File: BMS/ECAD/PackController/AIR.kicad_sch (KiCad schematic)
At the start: 0 parts

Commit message: did AIR monitoring circuit and started SDC CTRL / logik
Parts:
- added C401: 100nC 6V, Capacitor_SMD:C_0603_1608Metric, symbol Device:C
- added D401, D402: BAS16HT1G, Diode_SMD:D_SOD-323F, symbol Device:D
- added J1: Conn_01x08, symbol Connector_Generic:Conn_01x08
- added K401: AIR_P, symbol Relay:DIPxx-2Axx-21x
- added K402: AIR_N, symbol Relay:DIPxx-2Axx-21x
- added Q401, Q403: BC847C, Package_TO_SOT_SMD:SOT-23-3, symbol Transistor_BJT:Q_NPN_BEC
- added Q402, Q404: DMP4065S-7, Package_TO_SOT_SMD:SOT-23-3, symbol Transistor_FET:Q_PMOS_GSD
- added R401, R402, R407, R408, R409, R410, R411, R412, R413, R414: 1kR, Resistor_SMD:R_0603_1608Metric, symbol Device:R
- added R403, R405, R415, R417, R418, R419, R421, R422: 10kR, Resistor_SMD:R_0603_1608Metric, symbol Device:R
- added R404, R406: 1k5R, Resistor_SMD:R_0603_1608Metric, symbol Device:R
- added R416, R420: 4k7R, Resistor_SMD:R_0603_1608Metric, symbol Device:R
- added U401: ADCMP393ARUZ, symbol EKartParts:ADCMP393ARUZ
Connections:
- new net: R409.1, R410.2, U401.5 (+), U401.9 (+)
- new net: Q404.1 (G), R421.2, R422.1
- new net: Q403.3 (C), R422.2
- new net: R410.1, R411.2, U401.11 (+), U401.7 (+)
- new net: Q402.1 (G), R417.1, R418.2
- new net: Q401.3 (C), R417.2
- new net +3.3V: C401.1, R407.2, R408.2, R409.2, R412.2, R413.2, R414.2, U401.3 (VCC)
- new net AIR_Error: R412.1, U401.1, U401.13
- new net AIR_N_AUX1: J1.8 (Pin_8), K402.14, R407.1, U401.10 (-), U401.8 (-)
- new net AIR_N_AUX2: J1.4 (Pin_4), K402.8, R402.2
- new net AIR_N_Enable: D401.1 (K), J1.6 (Pin_6), K402.2, Q404.3 (D), R405.2
- new net AIR_N_Intended: R405.1, R406.1
- new net AIR_P_AUX1: J1.7 (Pin_7), K401.14, R408.1, U401.4 (-), U401.6 (-)
- new net AIR_P_AUX2: J1.3 (Pin_3), K401.8, R401.2
- new net AIR_P_Actual: R413.1, R414.1, U401.14, U401.2
- new net AIR_P_Enable: D402.1 (K), J1.5 (Pin_5), K401.2, Q402.3 (D), R403.2
- new net AIR_P_Intended: R403.1, R404.1
- new net GND: C401.2, D401.2 (A), D402.2 (A), J1.1 (Pin_1), J1.2 (Pin_2), K401.6, K402.6, Q401.2 (E), Q403.2 (E), R401.1, R402.1, R404.2, R406.2, R411.1, R415.2, R419.2, U401.12 (GND)
- new net SC_END: Q402.2 (S), Q404.2 (S), R418.1, R421.1
- new net TS_N_External: K402.7
- new net TS_N_Internal: K402.1
- new net TS_P_External: K401.7
- new net TS_P_Internal: K401.1
- new net ÂIR_N_Switch: R419.1, R420.2
- new net ÂIR_P_Switch: R415.1, R416.2

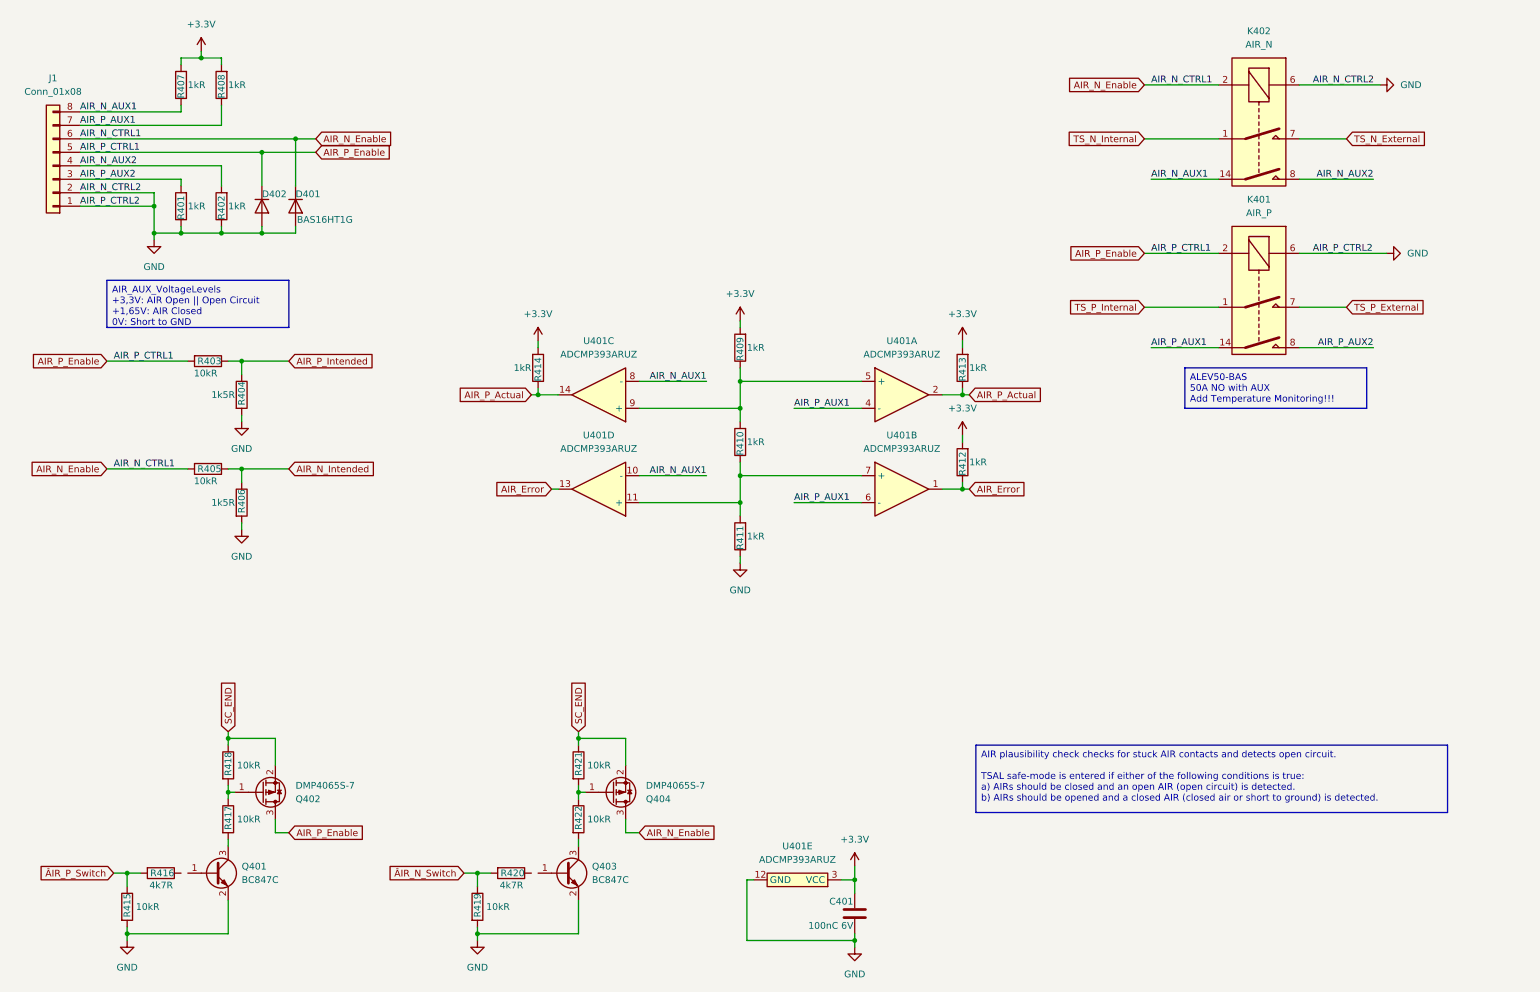
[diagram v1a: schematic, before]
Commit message: IMD control circuit
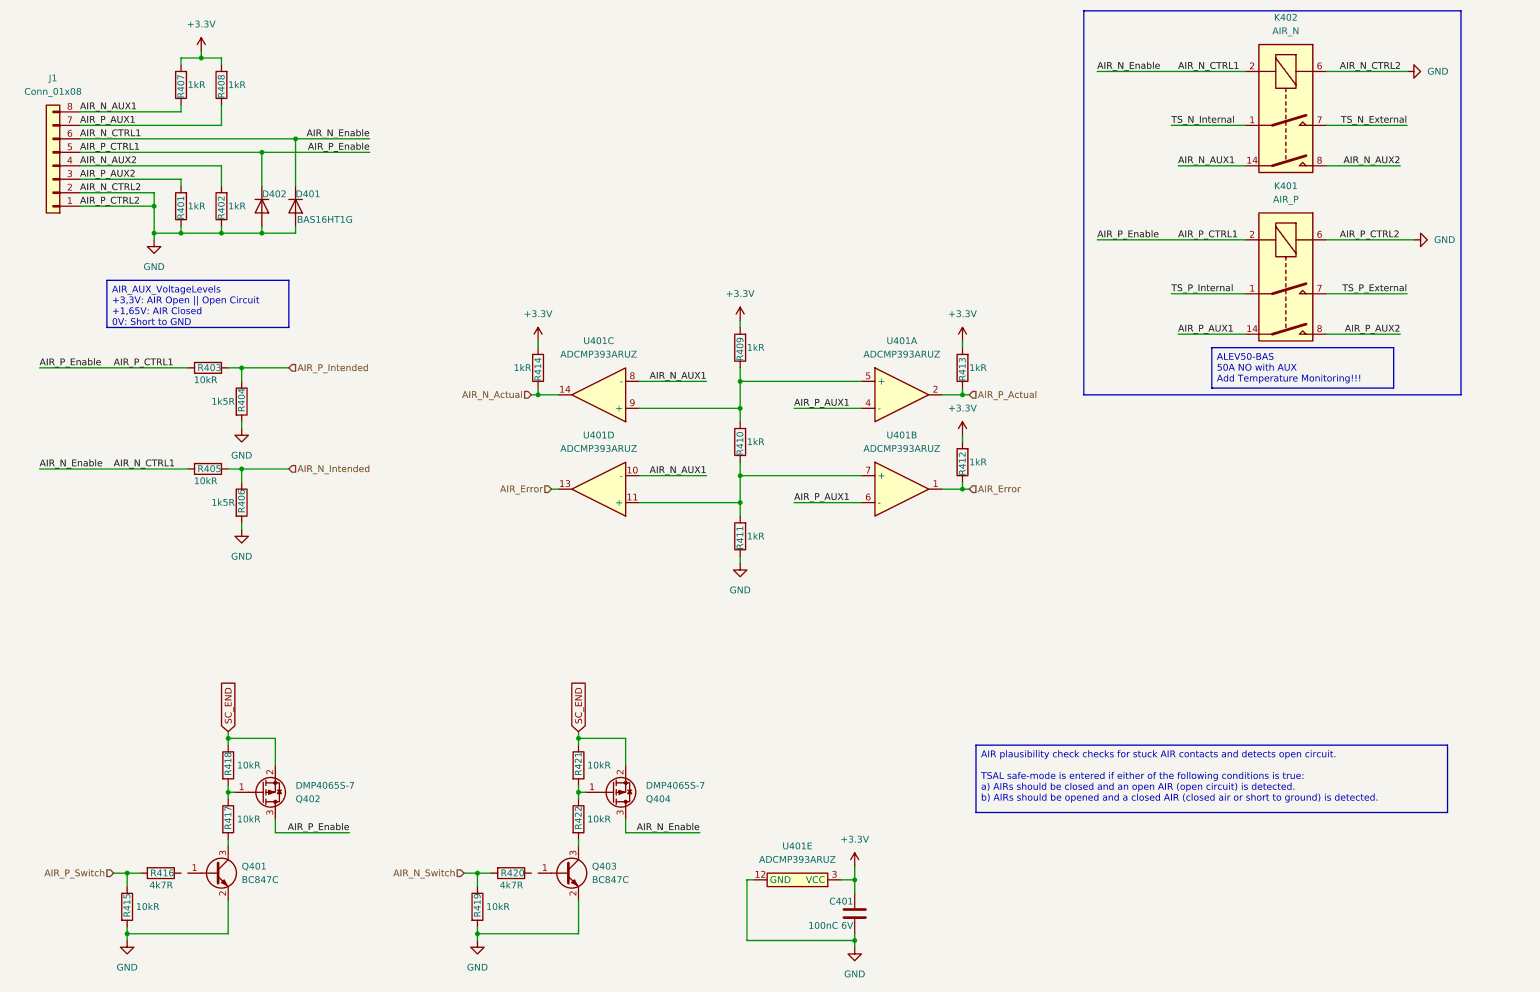
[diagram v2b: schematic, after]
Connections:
- net AIR_P_Actual: no longer R414.1, U401.14
- net AIR_N_Enable renamed AIR_N_CTRL1
- net AIR_P_Enable renamed AIR_P_CTRL1
- net ÂIR_N_Switch renamed AIR_N_Switch
- net ÂIR_P_Switch renamed AIR_P_Switch
- new net AIR_N_Actual: R414.1, U401.14
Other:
- moved on the sheet: K401, K402, R403, R404

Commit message: pack controller close to finished and startet pack controller
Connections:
- net at R420.1: now also Q403.1 (B)
- net at Q401.1 (B): now also R416.1

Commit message: finished schemativ of precharge
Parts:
- removed Q401, Q403: BC847C, Package_TO_SOT_SMD:SOT-23-3, symbol Transistor_BJT:Q_NPN_BEC
- added Q3, Q4: BC846, Package_TO_SOT_SMD:SOT-23, symbol Transistor_BJT:BC846
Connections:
- net GND: now also Q3.2 (E), Q4.2 (E)
- net at R422.2: now also Q4.3 (C)
- net at R420.1: now also Q4.1 (B)
- net at R416.1: now also Q3.1 (B)
- net at R417.2: now also Q3.3 (C)
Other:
- title: (none) -> PackController
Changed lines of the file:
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@@
 	(paper "A4")
 	(title_block
+		(title "PackController")
 		(date "2026-03-03")
 		(rev "V0.9")
@@
 		)
 	)
-	(global_label "SC_END"
+	(hierarchical_label "AIR_P_Actual"
 		(shape input)
-		(at 118.11 148.59 90)
-		(fields_autoplaced yes)
+		(at 191.77 85.09 0)
 		(effects
 			(font
@@
 			(justify left)
 		)
-		(property "Intersheetrefs" "${INTERSHEET_REFS}"
-			(at 118.11 138.4082 90)
-			(hide yes)
-			(show_name no)
-			(do_not_autoplace no)
-			(effects
-				(font
-					(size 1.27 1.27)
-				)
-				(justify left)
-			)
-		)
 	)
-	(global_label "SC_END"
+	(hierarchical_label "SC_END"
 		(shape input)
 		(at 52.07 148.59 90)
-		(fields_autoplaced yes)
 		(effects
 			(font
@@
 			(justify left)
 		)
-		(property "Intersheetrefs" "${INTERSHEET_REFS}"
-			(at 52.07 138.4082 90)
-			(hide yes)
-			(show_name no)
-			(do_not_autoplace no)
-			(effects
-				(font
-					(size 1.27 1.27)
-				)
-				(justify left)
-			)
-		)
 	)
-	(hierarchical_label "AIR_P_Actual"
+	(hierarchical_label "AIR_N_Actual"
 		(shape input)
-		(at 191.77 85.09 0)
+		(at 109.22 85.09 180)
 		(effects
 			(font
 				(size 1.27 1.27)
 			)
-			(justify left)
+			(justify right)
 		)
 	)
-	(hierarchical_label "AIR_N_Actual"
+	(hierarchical_label "SC_END"
 		(shape input)
-		(at 109.22 85.09 180)
+		(at 118.11 148.59 90)
 		(effects
 			(font
 				(size 1.27 1.27)
 			)
-			(justify right)
+			(justify left)
 		)
 	)
@@
 	)
 	(symbol
-		(lib_id "Transistor_BJT:Q_NPN_BEC")
+		(lib_id "Transistor_BJT:BC846")
 		(at 115.57 175.26 0)
 		(unit 1)
@@
 		(dnp no)
 		(fields_autoplaced yes)
-		(property "Reference" "Q403"
+		(property "Reference" "Q4"
 			(at 120.65 173.9899 0)
 			(show_name no)
@@
 			)
 		)
-		(property "Value" "BC847C"
+		(property "Value" "BC846"
 			(at 120.65 176.5299 0)
 			(show_name no)
@@
 			)
 		)
-		(property "Footprint" "Package_TO_SOT_SMD:SOT-23-3"
-			(at 120.65 172.72 0)
+		(property "Footprint" "Package_TO_SOT_SMD:SOT-23"
+			(at 120.65 177.165 0)
 			(hide yes)
 			(show_name no)
@@
 				(font
 					(size 1.27 1.27)
+					(italic yes)
 				)
+				(justify left)
 			)
 		)
-		(property "Datasheet" ""
+		(property "Datasheet" "https://assets.nexperia.com/documents/data-sheet/BC846_SER.pdf"
 			(at 115.57 175.26 0)
 			(hide yes)
@@
 					(size 1.27 1.27)
 				)
+				(justify left)
 			)
 		)
-		(property "Description" "NPN transistor, base/emitter/collector"
+		(property "Description" "0.1A Ic, 65V Vce, NPN Transistor, SOT-23"
 			(at 115.57 175.26 0)
 			(hide yes)
@@
 		(pin "2"
 		)
-		(pin "3"
-		)
 		(pin "1"
 		)
+		(pin "3"
+		)
 		(instances
 			(project "Pack_Controller"
 				(path "/58a1c93e-baba-4d23-9191-955e00968735/9e3af51c-36cf-42ea-bd79-21f3fecec64c"
-					(reference "Q403")
+					(reference "Q4")
 					(unit 1)
 				)
@@
 	)
 	(symbol
-		(lib_id "Transistor_BJT:Q_NPN_BEC")
-		(at 49.53 175.26 0)
-		(unit 1)
-		(body_style 1)
-		(exclude_from_sim no)
-		(in_bom yes)
-		(on_board yes)
-		(in_pos_files yes)
-		(dnp no)
-		(fields_autoplaced yes)
-		(property "Reference" "Q401"
-			(at 54.61 173.9899 0)
-			(show_name no)
-			(do_not_autoplace no)
-			(effects
-				(font
-					(size 1.27 1.27)
-				)
-				(justify left)
-			)
-		)
-		(property "Value" "BC847C"
-			(at 54.61 176.5299 0)
-			(show_name no)
-			(do_not_autoplace no)
-			(effects
-				(font
-					(size 1.27 1.27)
-				)
-				(justify left)
-			)
-		)
-		(property "Footprint" "Package_TO_SOT_SMD:SOT-23-3"
-			(at 54.61 172.72 0)
-			(hide yes)
-			(show_name no)
-			(do_not_autoplace no)
-			(effects
-				(font
-					(size 1.27 1.27)
-				)
-			)
-		)
-		(property "Datasheet" ""
-			(at 49.53 175.26 0)
-			(hide yes)
-			(show_name no)
-			(do_not_autoplace no)
-			(effects
-				(font
-					(size 1.27 1.27)
-				)
-			)
-		)
-		(property "Description" "NPN transistor, base/emitter/collector"
-			(at 49.53 175.26 0)
-			(hide yes)
-			(show_name no)
-			(do_not_autoplace no)
-			(effects
-				(font
-					(size 1.27 1.27)
-				)
-			)
-		)
-		(property "Sim.Device" "NPN"
-			(at 49.53 175.26 0)
-			(hide yes)
-			(show_name no)
-			(do_not_autoplace no)
-			(effects
-				(font
-					(size 1.27 1.27)
-				)
-			)
-		)
-		(property "Sim.Pins" "1=B 2=E 3=C"
-			(at 49.53 175.26 0)
-			(hide yes)
-			(show_name no)
-			(do_not_autoplace no)
-			(effects
-				(font
-					(size 1.27 1.27)
-				)
-			)
-		)
-		(pin "2"
-		)
-		(pin "3"
-		)
-		(pin "1"
-		)
-		(instances
-			(project "Pack_Controller"
-				(path "/58a1c93e-baba-4d23-9191-955e00968735/9e3af51c-36cf-42ea-bd79-21f3fecec64c"
-					(reference "Q401")
-					(unit 1)
-				)
-			)
-		)
-	)
-	(symbol
 		(lib_id "EKartParts:ADCMP393ARUZ")
 		(at 127 90.17 180)
@@
 					(unit 1)
 				)
+			)
+		)
+	)
+	(symbol
+		(lib_id "Transistor_BJT:BC846")
+		(at 49.53 175.26 0)
+		(unit 1)
+		(body_style 1)
+		(exclude_from_sim no)
+		(in_bom yes)
+		(on_board yes)
+		(in_pos_files yes)
+		(dnp no)
+		(fields_autoplaced yes)
+		(property "Reference" "Q3"
+			(at 54.61 173.9899 0)
+			(show_name no)
+			(do_not_autoplace no)
+			(effects
+				(font
+					(size 1.27 1.27)
+				)
+				(justify left)
+			)
+		)
+		(property "Value" "BC846"
+			(at 54.61 176.5299 0)
+			(show_name no)
+			(do_not_autoplace no)
+			(effects
+				(font
+					(size 1.27 1.27)
+				)
+				(justify left)
+			)
+		)
+		(property "Footprint" "Package_TO_SOT_SMD:SOT-23"
+			(at 54.61 177.165 0)
+			(hide yes)
+			(show_name no)
+			(do_not_autoplace no)
+			(effects
+				(font
+					(size 1.27 1.27)
+					(italic yes)
+				)
+				(justify left)
+			)
+		)
+		(property "Datasheet" "https://assets.nexperia.com/documents/data-sheet/BC846_SER.pdf"
+			(at 49.53 175.26 0)
+			(hide yes)
+			(show_name no)
+			(do_not_autoplace no)
+			(effects
+				(font
+					(size 1.27 1.27)
+				)
+				(justify left)
+			)
+		)
+		(property "Description" "0.1A Ic, 65V Vce, NPN Transistor, SOT-23"
+			(at 49.53 175.26 0)
+			(hide yes)
+			(show_name no)
+			(do_not_autoplace no)
+			(effects
+				(font
+					(size 1.27 1.27)
+				)
+			)
+		)
+		(property "Sim.Device" "NPN"
+			(at 49.53 175.26 0)
+			(hide yes)
+			(show_name no)
+			(do_not_autoplace no)
+			(effects
+				(font
+					(size 1.27 1.27)
+				)
+			)
+		)
+		(property "Sim.Pins" "1=B 2=E 3=C"
+			(at 49.53 175.26 0)
+			(hide yes)
+			(show_name no)
+			(do_not_autoplace no)
+			(effects
+				(font
+					(size 1.27 1.27)
+				)
+			)
+		)
+		(pin "2"
+		)
+		(pin "1"
+		)
+		(pin "3"
+		)
+		(instances
+			(project "Pack_Controller"
+				(path "/58a1c93e-baba-4d23-9191-955e00968735/9e3af51c-36cf-42ea-bd79-21f3fecec64c"
+					(reference "Q3")
+					(unit 1)
+				)
